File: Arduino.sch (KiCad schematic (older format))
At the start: 19 parts

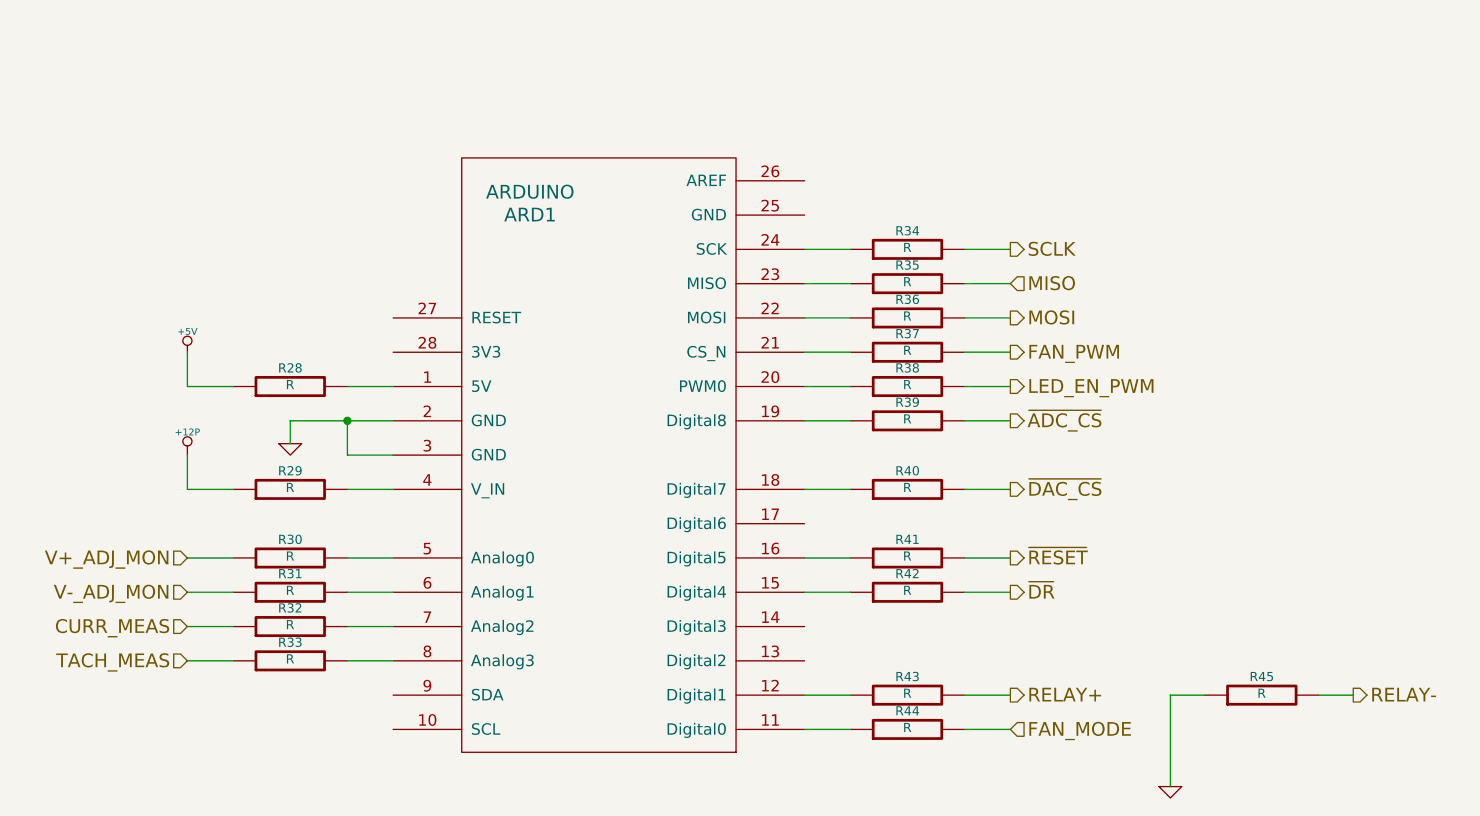
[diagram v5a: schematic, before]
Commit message: Initial layout of Arduino and Fan-Current
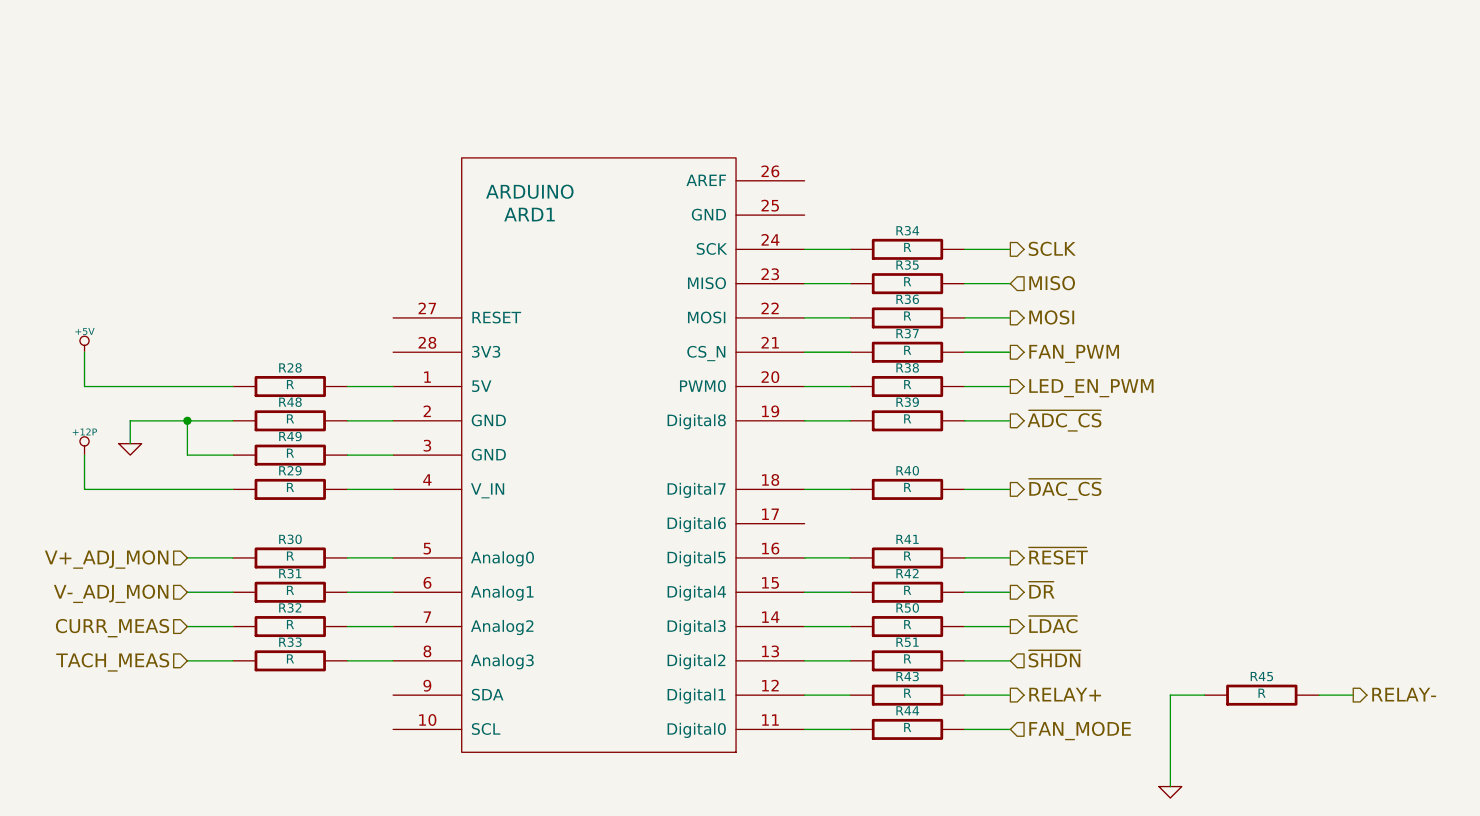
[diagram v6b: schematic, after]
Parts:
- added R48, R49, R50, R51: R, ~, symbol R
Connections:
- net GND: now also R48.1, R49.1; no longer ARD1.2 (GND), ARD1.3 (GND)
- net at ARD1.13 (Digital2): now also R51.1
- net at ARD1.14 (Digital3): now also R50.1
- new net: ARD1.2 (GND), R48.2
- new net: ARD1.3 (GND), R49.2
- new net ~LDAC: R50.2
- new net ~SHDN: R51.2
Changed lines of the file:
@@
 $Descr A4 11693 8268
 encoding utf-8
-Sheet 9 9
+Sheet 8 9
 Title ""
-Date "21 feb 2014"
+Date "22 feb 2014"
 Rev ""
 Comp ""
@@
 Text HLabel 4300 5050 0    60   Input ~ 0
 TACH_MEAS
-$Comp
-L ARDUINO ARD1
-U 1 1 52F3CC17
-P 6100 4150
-F 0 "ARD1" H 5800 5200 60  0000 C CNN
-F 1 "ARDUINO" H 5800 5300 60  0000 C CNN
-F 2 "~" H 6150 3600 60  0000 C CNN
-F 3 "~" H 6150 3600 60  0000 C CNN
-	1    6100 4150
-	1    0    0    -1
-$EndComp
 Wire Wire Line
 	7700 4300 7900 4300
@@
 	7200 5200 7000 5200
 $Comp
-L GND #PWR056
+L GND #PWR051
 U 1 1 52F3F486
 P 8600 5600
-F 0 "#PWR056" H 8600 5600 30  0001 C CNN
+F 0 "#PWR051" H 8600 5600 30  0001 C CNN
 F 1 "GND" H 8600 5530 30  0001 C CNN
 F 2 "" H 8600 5600 60  0000 C CNN
@@
 $EndComp
 Wire Wire Line
-	4500 4300 4300 4300
+	4500 4300 3850 4300
 Wire Wire Line
 	5000 4300 5200 4300
 $Comp
-L +12P #PWR057
+L +12P #PWR052
 U 1 1 52F4241E
-P 4300 4150
-F 0 "#PWR057" H 4300 4120 30  0001 C CNN
-F 1 "+12P" H 4300 4250 30  0000 C CNN
-F 2 "" H 4300 4150 60  0000 C CNN
-F 3 "" H 4300 4150 60  0000 C CNN
-	1    4300 4150
+P 3850 4150
+F 0 "#PWR052" H 3850 4120 30  0001 C CNN
+F 1 "+12P" H 3850 4250 30  0000 C CNN
+F 2 "" H 3850 4150 60  0000 C CNN
+F 3 "" H 3850 4150 60  0000 C CNN
+	1    3850 4150
 	1    0    0    -1
 $EndComp
 Wire Wire Line
-	4300 4300 4300 4150
+	3850 4300 3850 4150
 $Comp
 L R R28
@@
 $EndComp
 Wire Wire Line
-	4500 3850 4300 3850
+	4500 3850 3850 3850
 Wire Wire Line
 	5000 3850 5200 3850
 Wire Wire Line
-	4300 3850 4300 3700
-$Comp
-L +5V #PWR058
+	3850 3850 3850 3700
+$Comp
+L +5V #PWR053
 U 1 1 53010A7E
-P 4300 3700
-F 0 "#PWR058" H 4300 3790 20  0001 C CNN
-F 1 "+5V" H 4300 3790 30  0000 C CNN
-F 2 "~" H 4300 3700 60  0000 C CNN
-F 3 "~" H 4300 3700 60  0000 C CNN
-	1    4300 3700
+P 3850 3700
+F 0 "#PWR053" H 3850 3790 20  0001 C CNN
+F 1 "+5V" H 3850 3790 30  0000 C CNN
+F 2 "~" H 3850 3700 60  0000 C CNN
+F 3 "~" H 3850 3700 60  0000 C CNN
+	1    3850 3700
 	1    0    0    -1
 $EndComp
 $Comp
-L GND #PWR059
+L GND #PWR054
 U 1 1 53010A97
-P 4750 4100
-F 0 "#PWR059" H 4750 4100 30  0001 C CNN
-F 1 "GND" H 4750 4030 30  0001 C CNN
-F 2 "~" H 4750 4100 60  0000 C CNN
-F 3 "~" H 4750 4100 60  0000 C CNN
-	1    4750 4100
+P 4050 4100
+F 0 "#PWR054" H 4050 4100 30  0001 C CNN
+F 1 "GND" H 4050 4030 30  0001 C CNN
+F 2 "~" H 4050 4100 60  0000 C CNN
+F 3 "~" H 4050 4100 60  0000 C CNN
+	1    4050 4100
 	1    0    0    -1
 $EndComp
 Wire Wire Line
-	5200 4000 4750 4000
-Wire Wire Line
-	4750 4000 4750 4100
-Wire Wire Line
-	5200 4150 5000 4150
-Wire Wire Line
-	5000 4150 5000 4000
-Connection ~ 5000 4000
+	4050 4000 4500 4000
+Wire Wire Line
+	4050 4000 4050 4100
+Wire Wire Line
+	4300 4000 4300 4150
+Connection ~ 4300 4000
 Text HLabel 7900 4600 2    60   Output ~ 0
 ~RESET
@@
 Wire Wire Line
 	7200 4750 7000 4750
+$Comp
+L ARDUINO ARD1
+U 1 1 53080DCE
+P 6100 4150
+F 0 "ARD1" H 5800 5200 60  0000 C CNN
+F 1 "ARDUINO" H 5800 5300 60  0000 C CNN
+F 2 "~" H 6150 3600 60  0000 C CNN
+F 3 "~" H 6150 3600 60  0000 C CNN
+	1    6100 4150
+	1    0    0    -1
+$EndComp
+$Comp
+L R R48
+U 1 1 53081DC5
+P 4750 4000
+F 0 "R48" V 4830 4000 40  0000 C CNN
+F 1 "R" V 4757 4001 40  0000 C CNN
+F 2 "~" V 4680 4000 30  0000 C CNN
+F 3 "~" H 4750 4000 30  0000 C CNN
+	1    4750 4000
+	0    -1   -1   0
+$EndComp
+$Comp
+L R R49
+U 1 1 53081DCB
+P 4750 4150
+F 0 "R49" V 4830 4150 40  0000 C CNN
+F 1 "R" V 4757 4151 40  0000 C CNN
+F 2 "~" V 4680 4150 30  0000 C CNN
+F 3 "~" H 4750 4150 30  0000 C CNN
+	1    4750 4150
+	0    -1   -1   0
+$EndComp
+Wire Wire Line
+	5200 4000 5000 4000
+Wire Wire Line
+	5200 4150 5000 4150
+Wire Wire Line
+	4300 4150 4500 4150
+Text HLabel 7900 5050 2    60   Input ~ 0
+~SHDN
+Wire Wire Line
+	7700 5050 7900 5050
+$Comp
+L R R51
+U 1 1 530829A4
+P 7450 5050
+F 0 "R51" V 7530 5050 40  0000 C CNN
+F 1 "R" V 7457 5051 40  0000 C CNN
+F 2 "~" V 7380 5050 30  0000 C CNN
+F 3 "~" H 7450 5050 30  0000 C CNN
+	1    7450 5050
+	0    -1   -1   0
+$EndComp
+Wire Wire Line
+	7200 5050 7000 5050
+Text HLabel 7900 4900 2    60   Output ~ 0
+~LDAC
+Wire Wire Line
+	7700 4900 7900 4900
+$Comp
+L R R50
+U 1 1 530829AD
+P 7450 4900
+F 0 "R50" V 7530 4900 40  0000 C CNN
+F 1 "R" V 7457 4901 40  0000 C CNN
+F 2 "~" V 7380 4900 30  0000 C CNN
+F 3 "~" H 7450 4900 30  0000 C CNN
+	1    7450 4900
+	0    -1   -1   0
+$EndComp
+Wire Wire Line
+	7200 4900 7000 4900
 $EndSCHEMATC
